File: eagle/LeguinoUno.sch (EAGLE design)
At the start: 34 parts, among them Q1 60V/32A/35m?, Q2 60V/32A/35m?, Q3 60V/32A/35m?, Q4 60V/32A/35m?, Q5 60V/32A/35m?

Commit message: Updated EAGLE schematics and board, moved EAGLE files to top-level, created Gerber files.
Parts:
- EZSBC_PSU2-5: value (none) -> EzSBC PSU2-5
- Q1, Q2, Q3, Q4, Q5: value 60V/32A/35m? -> FQP30N06L
- renumbered U1 to EZSBC_PSU2-5

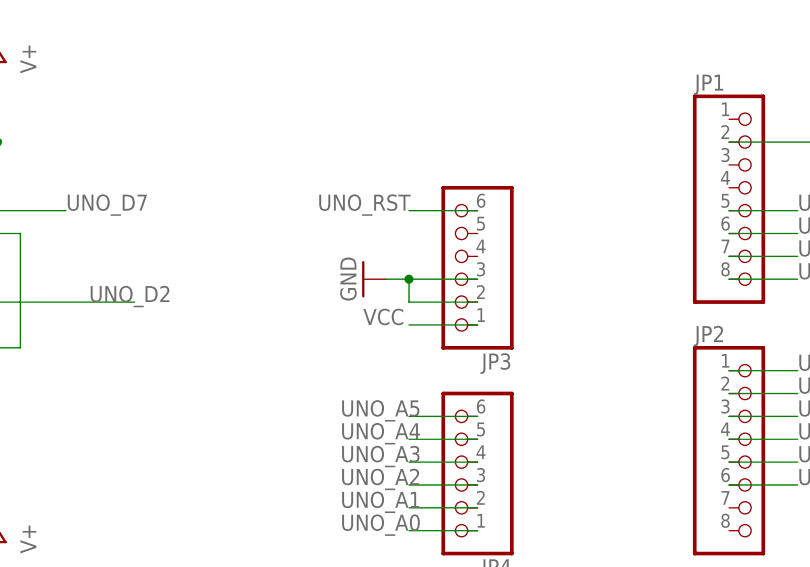
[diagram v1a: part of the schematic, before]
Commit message: fix VCC Arduino connection and width, reroute
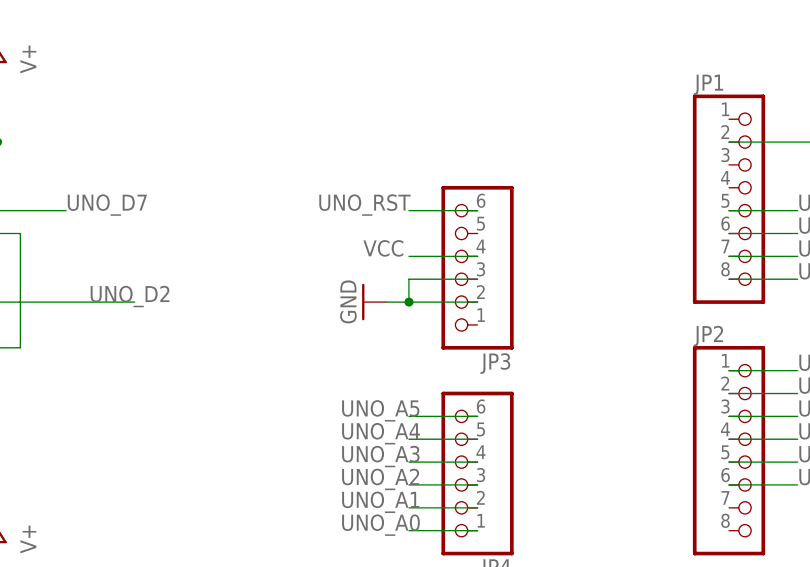
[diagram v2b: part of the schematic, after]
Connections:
- net VCC: now also JP3.4; no longer JP3.1
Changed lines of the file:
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@@
 <grid distance="0.1" unitdist="inch" unit="inch" style="lines" multiple="1" display="no" altdistance="0.01" altunitdist="inch" altunit="inch"/>
 <layers>
-<layer number="1" name="Top" color="4" fill="1" visible="yes" active="no"/>
-<layer number="16" name="Bottom" color="1" fill="1" visible="yes" active="no"/>
-<layer number="17" name="Pads" color="2" fill="1" visible="yes" active="no"/>
-<layer number="18" name="Vias" color="2" fill="1" visible="yes" active="no"/>
-<layer number="19" name="Unrouted" color="6" fill="1" visible="yes" active="no"/>
-<layer number="20" name="Dimension" color="24" fill="1" visible="yes" active="no"/>
-<layer number="21" name="tPlace" color="7" fill="1" visible="yes" active="no"/>
-<layer number="22" name="bPlace" color="7" fill="1" visible="yes" active="no"/>
-<layer number="23" name="tOrigins" color="15" fill="1" visible="yes" active="no"/>
-<layer number="24" name="bOrigins" color="15" fill="1" visible="yes" active="no"/>
-<layer number="25" name="tNames" color="7" fill="1" visible="yes" active="no"/>
-<layer number="26" name="bNames" color="7" fill="1" visible="yes" active="no"/>
-<layer number="27" name="tValues" color="7" fill="1" visible="yes" active="no"/>
-<layer number="28" name="bValues" color="7" fill="1" visible="yes" active="no"/>
+<layer number="1" name="Top" color="4" fill="1" visible="no" active="no"/>
+<layer number="16" name="Bottom" color="1" fill="1" visible="no" active="no"/>
+<layer number="17" name="Pads" color="2" fill="1" visible="no" active="no"/>
+<layer number="18" name="Vias" color="2" fill="1" visible="no" active="no"/>
+<layer number="19" name="Unrouted" color="6" fill="1" visible="no" active="no"/>
+<layer number="20" name="Dimension" color="24" fill="1" visible="no" active="no"/>
+<layer number="21" name="tPlace" color="7" fill="1" visible="no" active="no"/>
+<layer number="22" name="bPlace" color="7" fill="1" visible="no" active="no"/>
+<layer number="23" name="tOrigins" color="15" fill="1" visible="no" active="no"/>
+<layer number="24" name="bOrigins" color="15" fill="1" visible="no" active="no"/>
+<layer number="25" name="tNames" color="7" fill="1" visible="no" active="no"/>
+<layer number="26" name="bNames" color="7" fill="1" visible="no" active="no"/>
+<layer number="27" name="tValues" color="7" fill="1" visible="no" active="no"/>
+<layer number="28" name="bValues" color="7" fill="1" visible="no" active="no"/>
 <layer number="29" name="tStop" color="7" fill="3" visible="no" active="no"/>
 <layer number="30" name="bStop" color="7" fill="6" visible="no" active="no"/>
@@
 <layer number="35" name="tGlue" color="7" fill="4" visible="no" active="no"/>
 <layer number="36" name="bGlue" color="7" fill="5" visible="no" active="no"/>
-<layer number="37" name="tTest" color="7" fill="1" visible="yes" active="no"/>
-<layer number="38" name="bTest" color="7" fill="1" visible="yes" active="no"/>
+<layer number="37" name="tTest" color="7" fill="1" visible="no" active="no"/>
+<layer number="38" name="bTest" color="7" fill="1" visible="no" active="no"/>
 <layer number="39" name="tKeepout" color="4" fill="11" visible="no" active="no"/>
 <layer number="40" name="bKeepout" color="1" fill="11" visible="no" active="no"/>
@@
 <layer number="44" name="Drills" color="7" fill="1" visible="no" active="no"/>
 <layer number="45" name="Holes" color="7" fill="1" visible="no" active="no"/>
-<layer number="46" name="Milling" color="3" fill="1" visible="yes" active="no"/>
-<layer number="47" name="Measures" color="7" fill="1" visible="yes" active="no"/>
-<layer number="48" name="Document" color="7" fill="1" visible="yes" active="no"/>
-<layer number="49" name="Reference" color="7" fill="1" visible="yes" active="no"/>
-<layer number="50" name="dxf" color="7" fill="1" visible="yes" active="no"/>
-<layer number="51" name="tDocu" color="7" fill="1" visible="yes" active="no"/>
-<layer number="52" name="bDocu" color="7" fill="1" visible="yes" active="no"/>
-<layer number="53" name="tGND_GNDA" color="7" fill="9" visible="yes" active="no"/>
-<layer number="54" name="bGND_GNDA" color="1" fill="9" visible="yes" active="no"/>
-<layer number="56" name="wert" color="7" fill="1" visible="yes" active="no"/>
-<layer number="57" name="tCAD" color="7" fill="1" visible="yes" active="no"/>
-<layer number="59" name="tCarbon" color="7" fill="1" visible="yes" active="no"/>
-<layer number="60" name="bCarbon" color="7" fill="1" visible="yes" active="no"/>
+<layer number="46" name="Milling" color="3" fill="1" visible="no" active="no"/>
+<layer number="47" name="Measures" color="7" fill="1" visible="no" active="no"/>
+<layer number="48" name="Document" color="7" fill="1" visible="no" active="no"/>
+<layer number="49" name="Reference" color="7" fill="1" visible="no" active="no"/>
+<layer number="50" name="dxf" color="7" fill="1" visible="no" active="no"/>
+<layer number="51" name="tDocu" color="7" fill="1" visible="no" active="no"/>
+<layer number="52" name="bDocu" color="7" fill="1" visible="no" active="no"/>
+<layer number="53" name="tGND_GNDA" color="7" fill="9" visible="no" active="no"/>
+<layer number="54" name="bGND_GNDA" color="1" fill="9" visible="no" active="no"/>
+<layer number="56" name="wert" color="7" fill="1" visible="no" active="no"/>
+<layer number="57" name="tCAD" color="7" fill="1" visible="no" active="no"/>
+<layer number="59" name="tCarbon" color="7" fill="1" visible="no" active="no"/>
+<layer number="60" name="bCarbon" color="7" fill="1" visible="no" active="no"/>
 <layer number="88" name="SimResults" color="9" fill="1" visible="yes" active="yes"/>
 <layer number="89" name="SimProbes" color="9" fill="1" visible="yes" active="yes"/>
@@
 <instance part="JP3" gate="A" x="99.06" y="76.2" rot="R180"/>
 <instance part="JP4" gate="A" x="99.06" y="53.34" rot="R180"/>
-<instance part="GND12" gate="1" x="88.9" y="73.66" rot="R270"/>
+<instance part="GND12" gate="1" x="88.9" y="71.12" rot="R270"/>
 <instance part="GND13" gate="1" x="142.24" y="88.9" rot="R90"/>
 <instance part="NANO_VIN1" gate="VCC" x="-7.62" y="139.7" rot="R90"/>
@@
 </segment>
 <segment>
-<pinref part="JP3" gate="A" pin="3"/>
-<pinref part="GND12" gate="1" pin="GND"/>
-<wire x1="101.6" y1="73.66" x2="93.98" y2="73.66" width="0.1524" layer="91"/>
-<pinref part="JP3" gate="A" pin="2"/>
-<wire x1="93.98" y1="73.66" x2="91.44" y2="73.66" width="0.1524" layer="91"/>
-<wire x1="101.6" y1="71.12" x2="93.98" y2="71.12" width="0.1524" layer="91"/>
-<wire x1="93.98" y1="73.66" x2="93.98" y2="71.12" width="0.1524" layer="91"/>
-<junction x="93.98" y="73.66"/>
-</segment>
-<segment>
 <pinref part="JP1" gate="A" pin="2"/>
 <pinref part="GND13" gate="1" pin="GND"/>
 <wire x1="129.54" y1="88.9" x2="139.7" y2="88.9" width="0.1524" layer="91"/>
 </segment>
-</net>
-<net name="N$1" class="0">
+<segment>
+<pinref part="JP3" gate="A" pin="3"/>
+<wire x1="101.6" y1="73.66" x2="93.98" y2="73.66" width="0.1524" layer="91"/>
+<pinref part="JP3" gate="A" pin="2"/>
+<wire x1="101.6" y1="71.12" x2="93.98" y2="71.12" width="0.1524" layer="91"/>
+<wire x1="93.98" y1="73.66" x2="93.98" y2="71.12" width="0.1524" layer="91"/>
+<pinref part="GND12" gate="1" pin="GND"/>
+<wire x1="91.44" y1="71.12" x2="93.98" y2="71.12" width="0.1524" layer="91"/>
+<junction x="93.98" y="71.12"/>
+</segment>
+</net>
+<net name="N$1" class="1">
 <segment>
 <pinref part="EZSBC_PSU2-5" gate="G$1" pin="IN"/>
@@
 </segment>
 </net>
-<net name="VCC" class="0">
+<net name="VCC" class="1">
 <segment>
 <pinref part="EZSBC_PSU2-5" gate="G$1" pin="OUT"/>
@@
 <wire x1="187.96" y1="149.86" x2="190.5" y2="149.86" width="0.1524" layer="91"/>
 <junction x="187.96" y="149.86"/>
-</segment>
-<segment>
-<pinref part="JP3" gate="A" pin="1"/>
-<wire x1="101.6" y1="68.58" x2="93.98" y2="68.58" width="0.1524" layer="91"/>
-<label x="88.9" y="68.58" size="1.778" layer="95"/>
 </segment>
 <segment>
@@
 <pinref part="NANO_VIN1" gate="VCC" pin="VCC"/>
 </segment>
-</net>
+<segment>
+<pinref part="JP3" gate="A" pin="4"/>
+<wire x1="93.98" y1="76.2" x2="101.6" y2="76.2" width="0.1524" layer="91"/>
+<label x="88.9" y="76.2" size="1.778" layer="95"/>
+</segment>
+</net>

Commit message: fix analog pin assignment for Uno
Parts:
- renumbered PWR to POWER, RST to RESET
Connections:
- net UNO_A0: now also JP4.6; no longer JP4.1
- net UNO_A1: now also JP4.5; no longer JP4.2
- net UNO_A2: now also JP4.4; no longer JP4.3
- net UNO_A3: now also JP4.3; no longer JP4.4
- net UNO_A4: now also JP4.2; no longer JP4.5
- net UNO_A5: now also JP4.1; no longer JP4.6
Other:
- moved on the sheet: IN_1, IN_2, IN_3, IN_4, IN_5, IN_6
